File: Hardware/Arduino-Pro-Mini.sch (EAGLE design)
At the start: 26 parts, among them Q1 8/16MHz, U1 ATMEGA328, U2 MIC5205

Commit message: Post review and checklist verification
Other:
- note added: "Place 3.3V Reg. for 8MHz Place 5.0V Reg for 16MHz"
- note added: "Place 8MHz XTAL for 3.3V Place 16MHz XTAL for 5.0V"
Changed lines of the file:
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@@
 I2C Pull-ups</text>
 <text x="240.284" y="7.366" size="2.54" layer="94" font="vector">16</text>
-<text x="7.62" y="119.38" size="1.778" layer="97" font="vector" align="top-left">Power isolation jumper SJ1:
+<text x="50.8" y="114.3" size="1.778" layer="97" font="vector" align="top-left">Power isolation jumper SJ1:
  Open to source mini from
  alternate supply.  Usually
@@
 <wire x1="104.14" y1="127" x2="104.14" y2="53.34" width="0.1524" layer="97" style="longdash"/>
 <wire x1="0" y1="127" x2="104.14" y2="127" width="0.1524" layer="97" style="longdash"/>
-<text x="147.32" y="167.64" size="3.175" layer="97" font="vector">Microcontroller</text>
+<text x="149.86" y="172.72" size="3.175" layer="97" font="vector">Microcontroller</text>
 <rectangle x1="224.1741" y1="36.7094" x2="224.2757" y2="36.7221" layer="94"/>
 <rectangle x1="224.1614" y1="36.7221" x2="224.2884" y2="36.7348" layer="94"/>
@@
 Arduino Pro Mini Design by SparkFun Electronics
 Revised by: Marshall Taylor</text>
+<text x="152.4" y="170.18" size="1.778" layer="97" font="vector" align="top-left">Place 8MHz XTAL for 3.3V
+Place 16MHz XTAL for 5.0V</text>
+<text x="7.62" y="119.38" size="1.778" layer="97" font="vector" align="top-left">Place 3.3V Reg. for 8MHz
+Place 5.0V Reg for 16MHz</text>
 </plain>
 <instances>
@@
 <attribute name="VALUE" x="66.04" y="91.44" size="1.778" layer="96"/>
 </instance>
-<instance part="P+4" gate="G$1" x="86.36" y="99.06" smashed="yes">
-<attribute name="VALUE" x="85.344" y="102.616" size="1.778" layer="96" font="vector"/>
+<instance part="P+4" gate="G$1" x="96.52" y="99.06" smashed="yes">
+<attribute name="VALUE" x="95.504" y="102.616" size="1.778" layer="96" font="vector"/>
 </instance>
 <instance part="S1" gate="G$1" x="124.46" y="142.24" smashed="yes" rot="R90">
@@
 <segment>
 <pinref part="P+4" gate="G$1" pin="3.3V"/>
-<wire x1="86.36" y1="99.06" x2="86.36" y2="96.52" width="0.1524" layer="91"/>
+<wire x1="96.52" y1="99.06" x2="96.52" y2="96.52" width="0.1524" layer="91"/>
 <pinref part="SJ1" gate="1" pin="2"/>
-<wire x1="86.36" y1="96.52" x2="83.82" y2="96.52" width="0.1524" layer="91"/>
+<wire x1="96.52" y1="96.52" x2="83.82" y2="96.52" width="0.1524" layer="91"/>
 <pinref part="C13" gate="G$1" pin="+"/>
 <wire x1="83.82" y1="96.52" x2="76.2" y2="96.52" width="0.1524" layer="91"/>

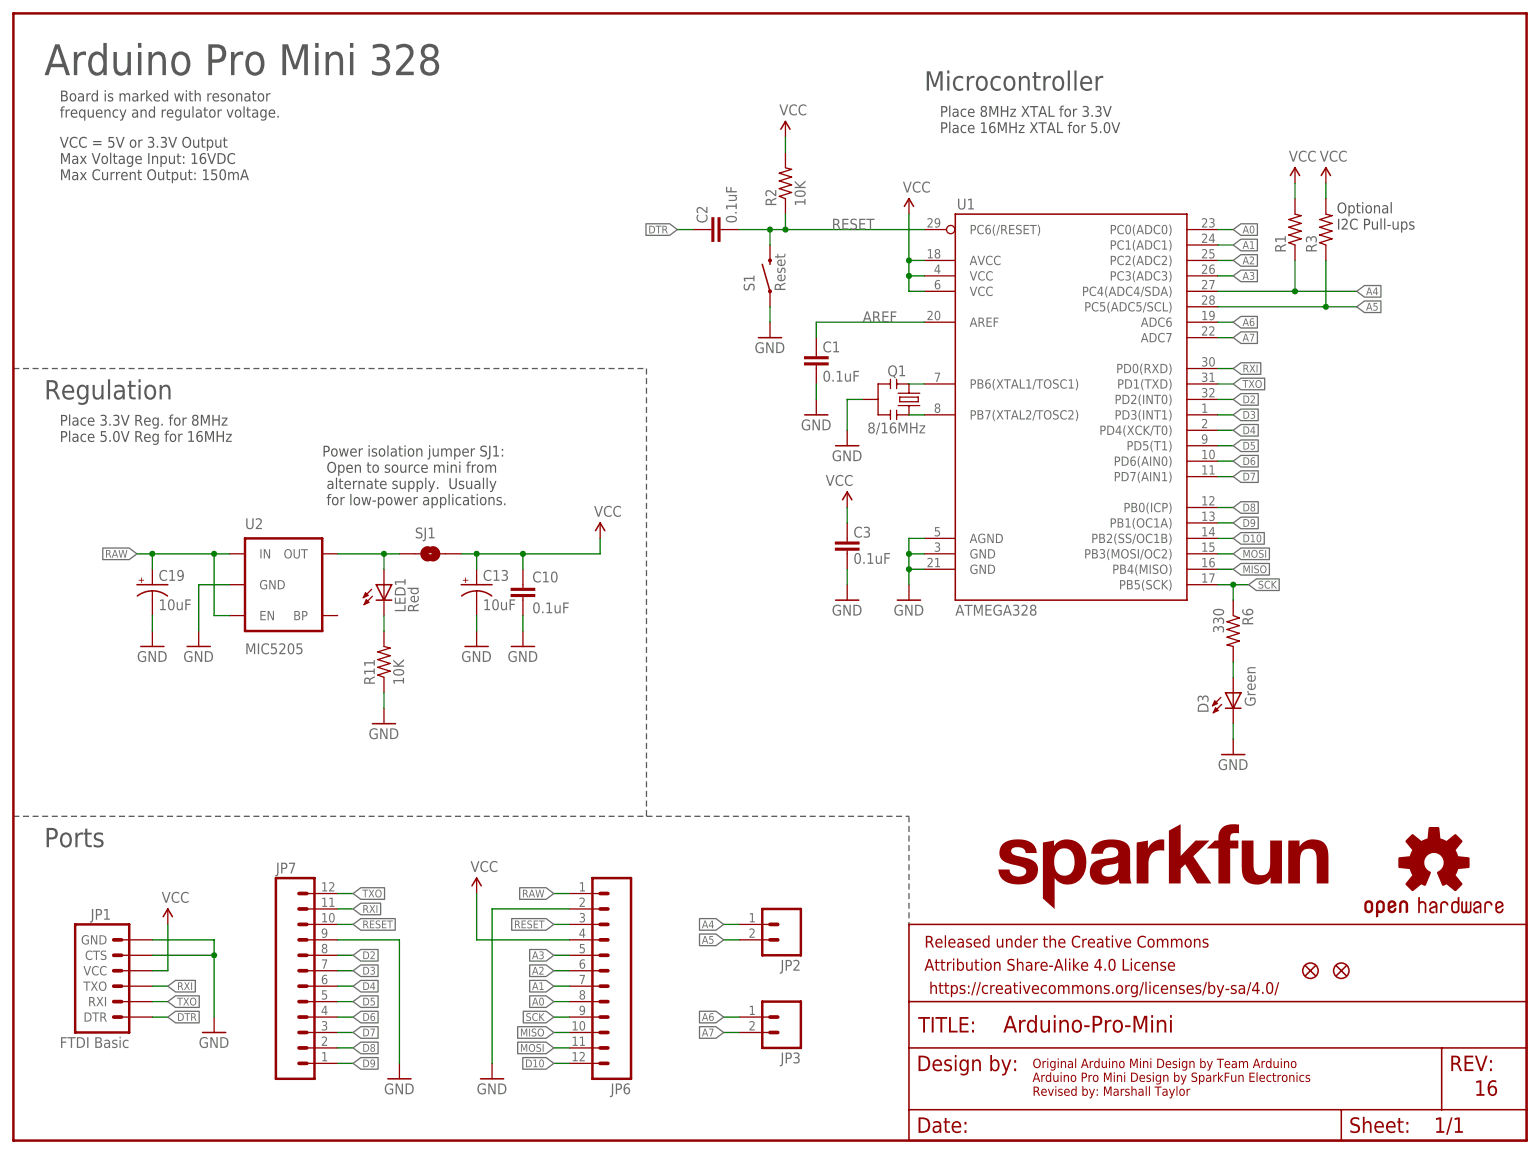
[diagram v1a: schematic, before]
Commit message: Added dual-part SKU information in schematic
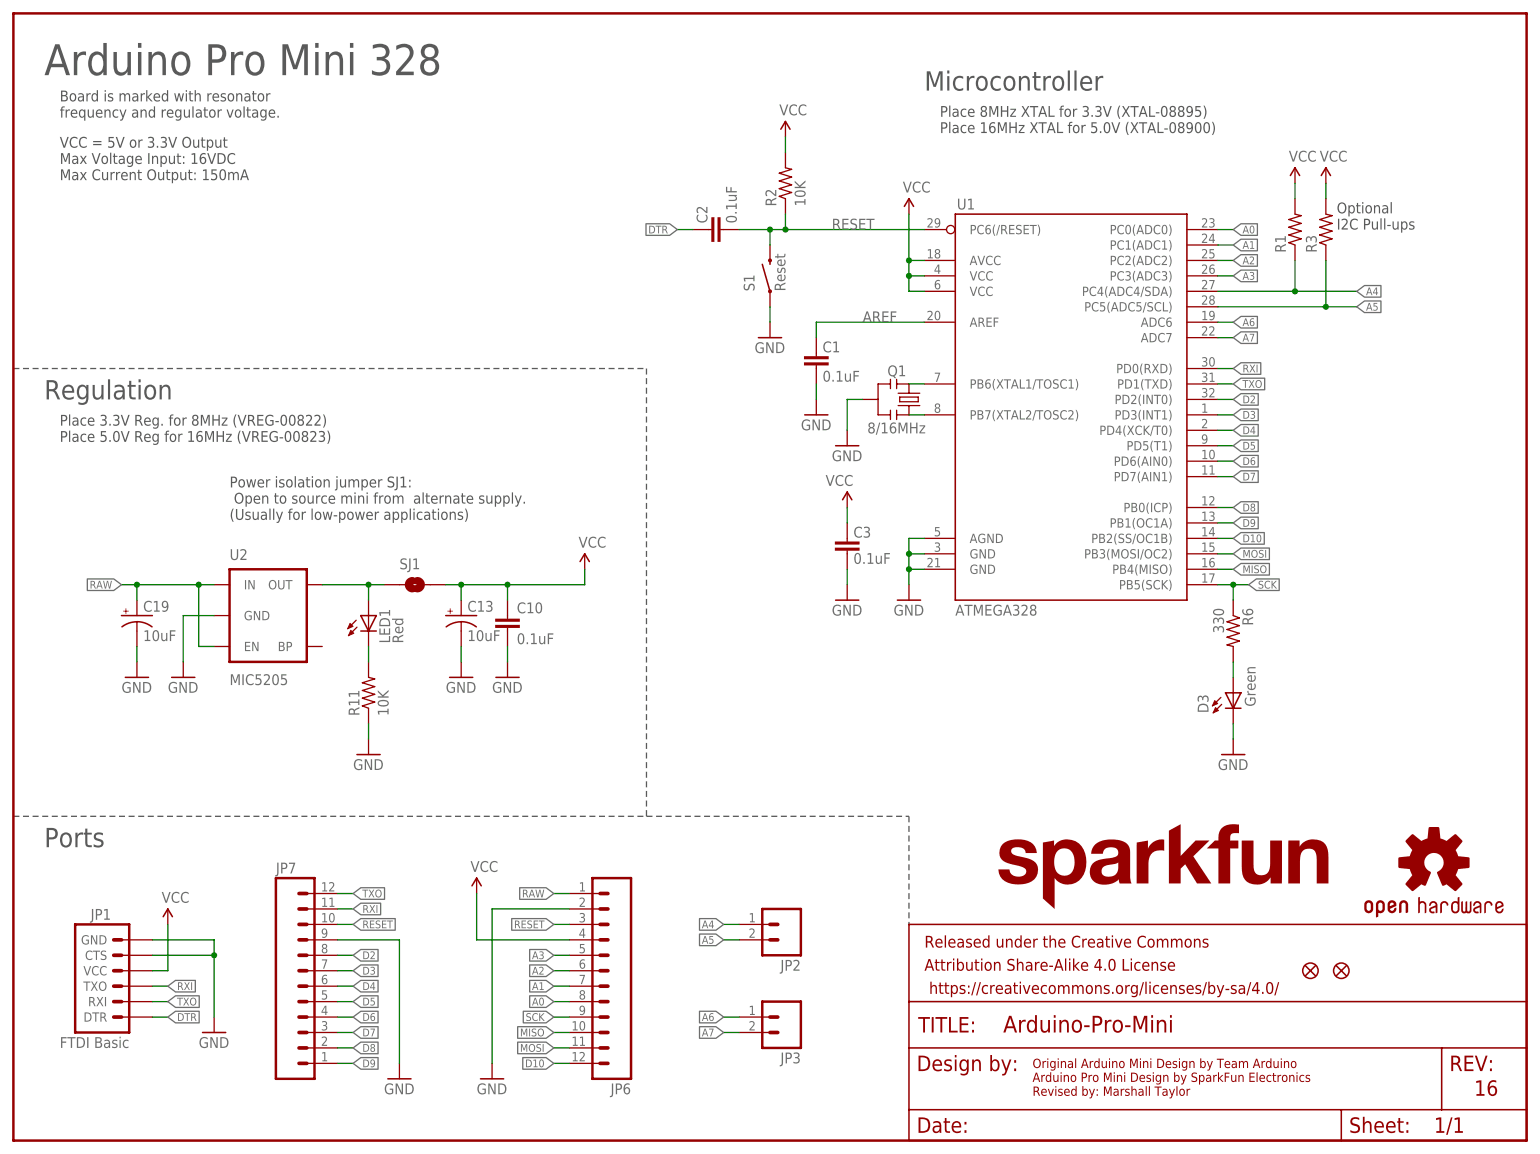
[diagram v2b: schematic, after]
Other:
- note added: "Place 3.3V Reg. for 8MHz (VREG-00822) Place 5.0V Reg for 16MHz (VREG-00823)"
- note added: "Place 8MHz XTAL for 3.3V (XTAL-08895) Place 16MHz XTAL for 5.0V (XTAL-08900)"
- note added: "Power isolation jumper SJ1: Open to source mini from alternate supply. (Usually for low-power applications)"
- note removed: "Place 3.3V Reg. for 8MHz Place 5.0V Reg for 16MHz"
- note removed: "Place 8MHz XTAL for 3.3V Place 16MHz XTAL for 5.0V"
- note removed: "Power isolation jumper SJ1: Open to source mini from alternate supply. Usually for low-power applications."
- moved on the sheet: C10, C13, C19, LED1, R11, SJ1, U2

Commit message: Incremented version numbers
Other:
- note added: "v20"
- note removed: "16"
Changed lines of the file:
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@@
 <text x="217.678" y="149.86" size="1.778" layer="97" font="vector">Optional
 I2C Pull-ups</text>
-<text x="240.284" y="7.366" size="2.54" layer="94" font="vector">16</text>
+<text x="240.284" y="7.366" size="2.54" layer="94" font="vector">v20</text>
 <text x="35.56" y="109.22" size="1.778" layer="97" font="vector" align="top-left">Power isolation jumper SJ1:
  Open to source mini from  alternate supply.
